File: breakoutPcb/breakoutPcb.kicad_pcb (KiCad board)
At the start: 2 copper layers, 49 x 49 mm, 18 parts, among them J1 DB9_Female_MountingHoles, J2 ConY1, J3 ConY2, J4 ConX1, J5 ConX2

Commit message: Matching adapted to reality
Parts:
- removed REF** (x2): MountingHole_3.2mm_M3_DIN965_Pad, MountingHole:MountingHole_3.2mm_M3_DIN965_Pad
- L1, L2, L3, L4: footprint Inductor_SMD:L_1008_2520Metric -> Wurth:Wurth4035

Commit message: Back copper is now also GND ...
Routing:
- added copper zone on B.Cu, net GND
- removed copper zone on B.Cu, net (none)

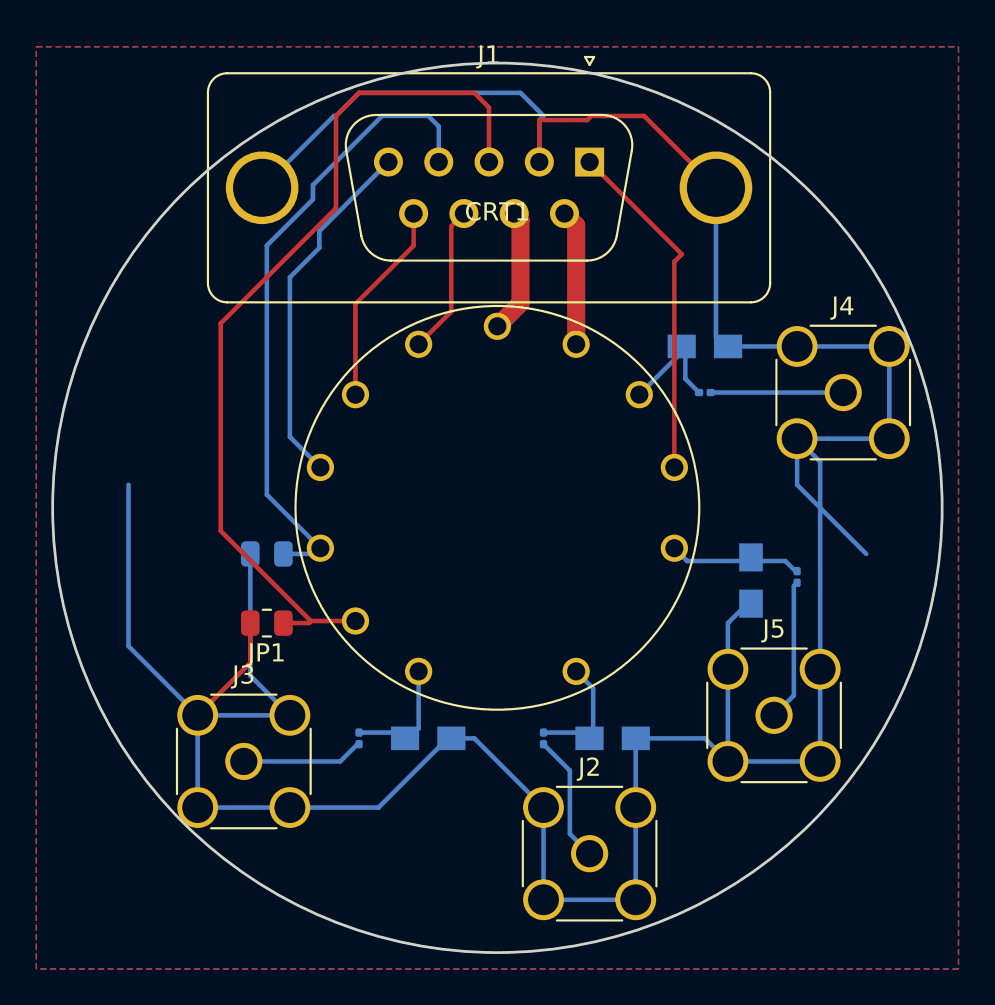
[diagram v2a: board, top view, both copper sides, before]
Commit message: Vanished mounting holes
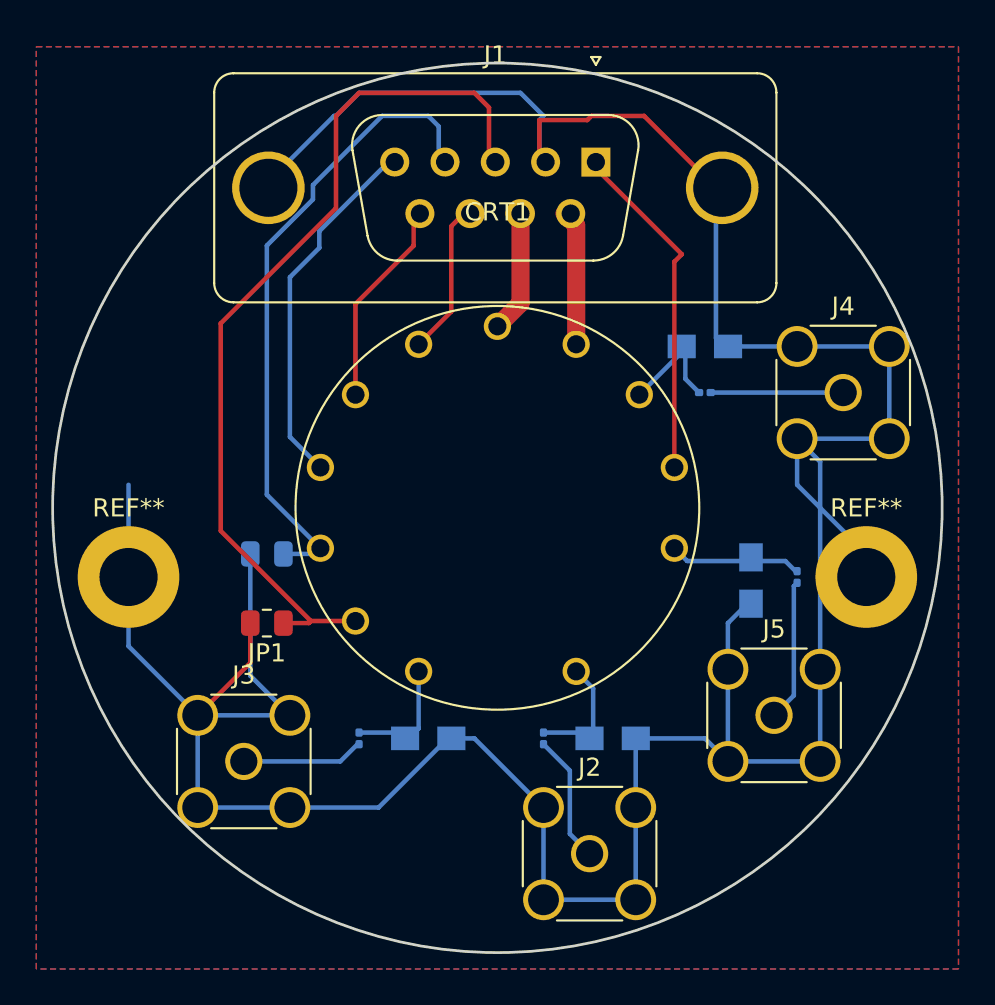
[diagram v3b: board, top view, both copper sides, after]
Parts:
- added REF**: MountingHole_3.2mm_M3_DIN965_Pad, MountingHole:MountingHole_3.2mm_M3_DIN965_Pad, F.Cu at (55.9, 80.0)
- added REF**: MountingHole_3.2mm_M3_DIN965_Pad, MountingHole:MountingHole_3.2mm_M3_DIN965_Pad, F.Cu at (96.5, 80.0)
- moved J1 0.34 mm to (81.6, 57.1)

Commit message: Symmetrized layout, changed connector assignment
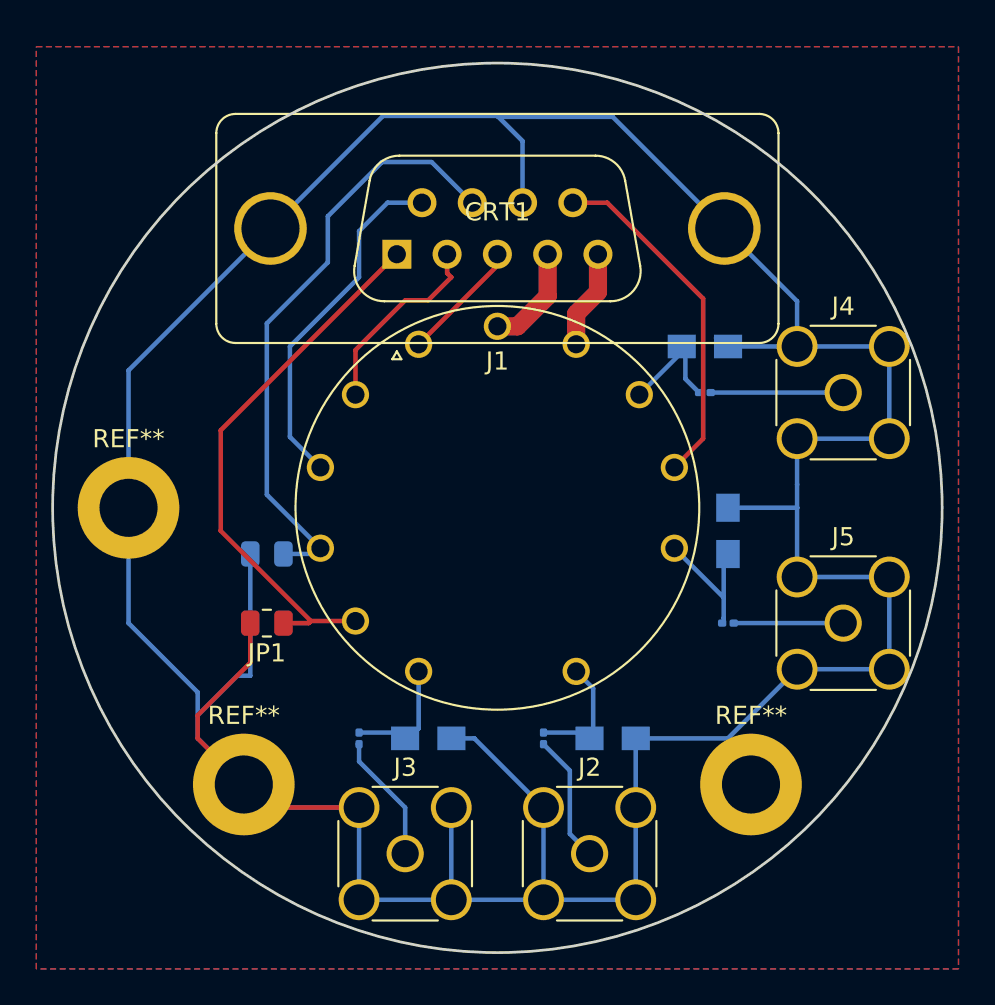
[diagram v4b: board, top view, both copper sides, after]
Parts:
- removed the REF** at (55.9, 80.0)
- removed the REF** at (96.5, 80.0)
- added REF**: MountingHole_3.2mm_M3_DIN965_Pad, MountingHole:MountingHole_3.2mm_M3_DIN965_Pad, F.Cu at (62.2, 91.4)
- added REF**: MountingHole_3.2mm_M3_DIN965_Pad, MountingHole:MountingHole_3.2mm_M3_DIN965_Pad, F.Cu at (90.2, 91.4)
- added REF**: MountingHole_3.2mm_M3_DIN965_Pad, MountingHole:MountingHole_3.2mm_M3_DIN965_Pad, F.Cu at (55.9, 76.2)
- C1, C2, C3, C4: value 13 pF -> 18 pF
- L1, L2, L3, L4: value 45 nH -> 70 nH
- moved J1 12.1 mm to (70.7, 62.2), turned to 180 degrees
- moved J3 10.2 mm to (71.1, 95.2)
- moved J5 6.35 mm to (95.2, 82.5)
- moved C4 4.58 mm to (88.9, 82.5), turned to 180 degrees
- moved L3 3.02 mm to (88.9, 77.5), turned to 90 degrees
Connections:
- J1 pad 1: Net-(CRT1-Pad12) -> Net-(CRT1-Pad6)
- J1 pad 2: GND -> Net-(CRT1-Pad3)
- J1 pad 3: Net-(CRT1-Pad6) -> Net-(CRT1-Pad2)
- J1 pad 4: Net-(CRT1-Pad5) -> Net-(CRT1-Pad1)
- J1 pad 5: Net-(CRT1-Pad4) -> Net-(CRT1-Pad14)
- J1 pad 6: Net-(CRT1-Pad14) -> Net-(CRT1-Pad4)
- J1 pad 7: Net-(CRT1-Pad1) -> Net-(CRT1-Pad5)
- J1 pad 8: Net-(CRT1-Pad2) -> GND
- J1 pad 9: Net-(CRT1-Pad3) -> Net-(CRT1-Pad12)
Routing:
- net GND: track 191.5 -> 219.4 mm
- net Net-(CRT1-Pad6): track 48.8 -> 30.3 mm
- net Net-(CRT1-Pad14): track 7.47 -> 5.46 mm
- net Net-(CRT1-Pad5): track 35.2 -> 33.2 mm
- net Net-(C4-Pad1): track 7.83 -> 6.03 mm
- net Net-(CRT1-Pad2): track 8.23 -> 6.76 mm
- net Net-(CRT1-Pad1): track 6.88 -> 5.77 mm
- net Net-(CRT1-Pad3): track 11.3 -> 10.8 mm
